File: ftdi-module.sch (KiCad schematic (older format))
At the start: 42 parts, among them J1 WE_629105150521, U1 FT2232HL-REEL, U2 NCP163ASN330T1G, Y1 KX-7_12,MHz

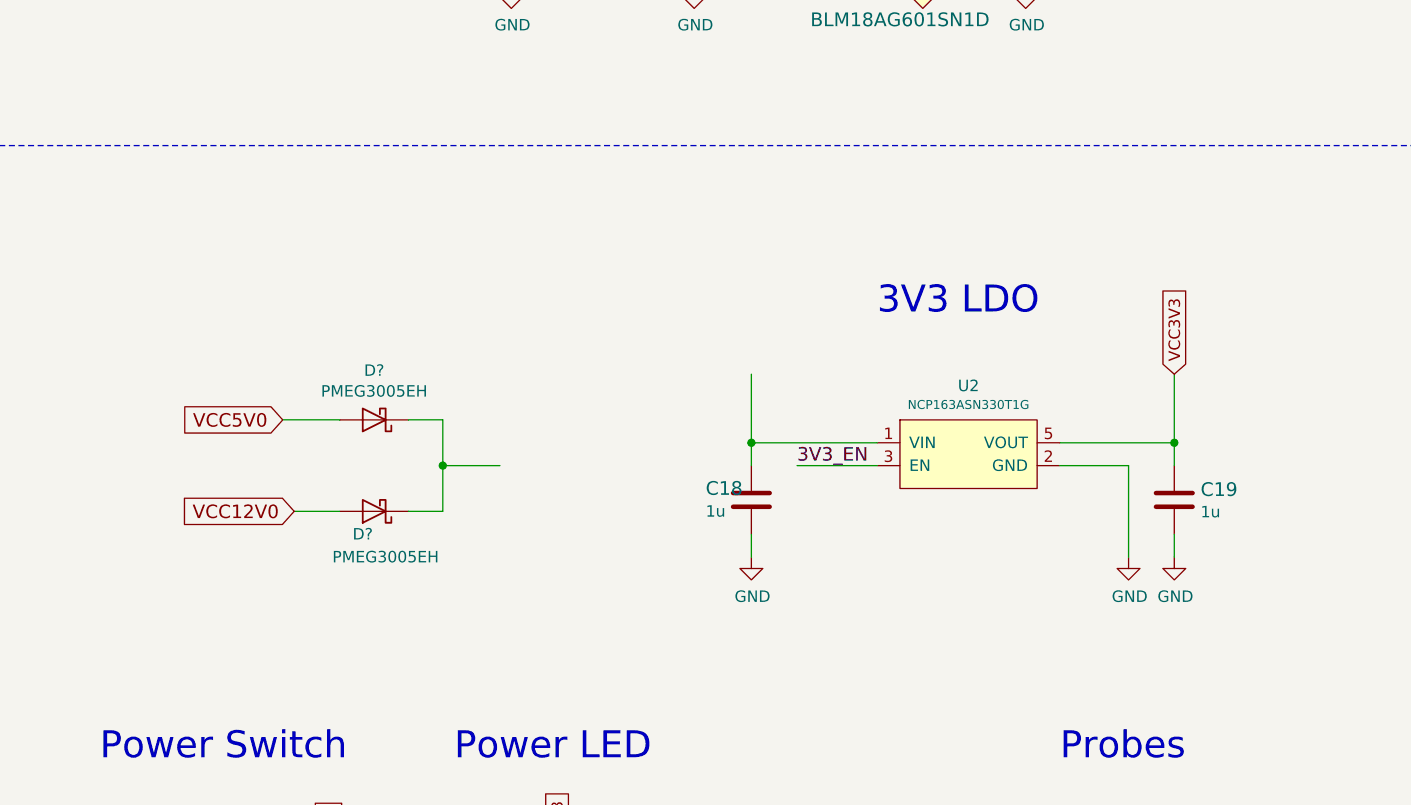
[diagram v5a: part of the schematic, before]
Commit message: Added connection between breakout boards
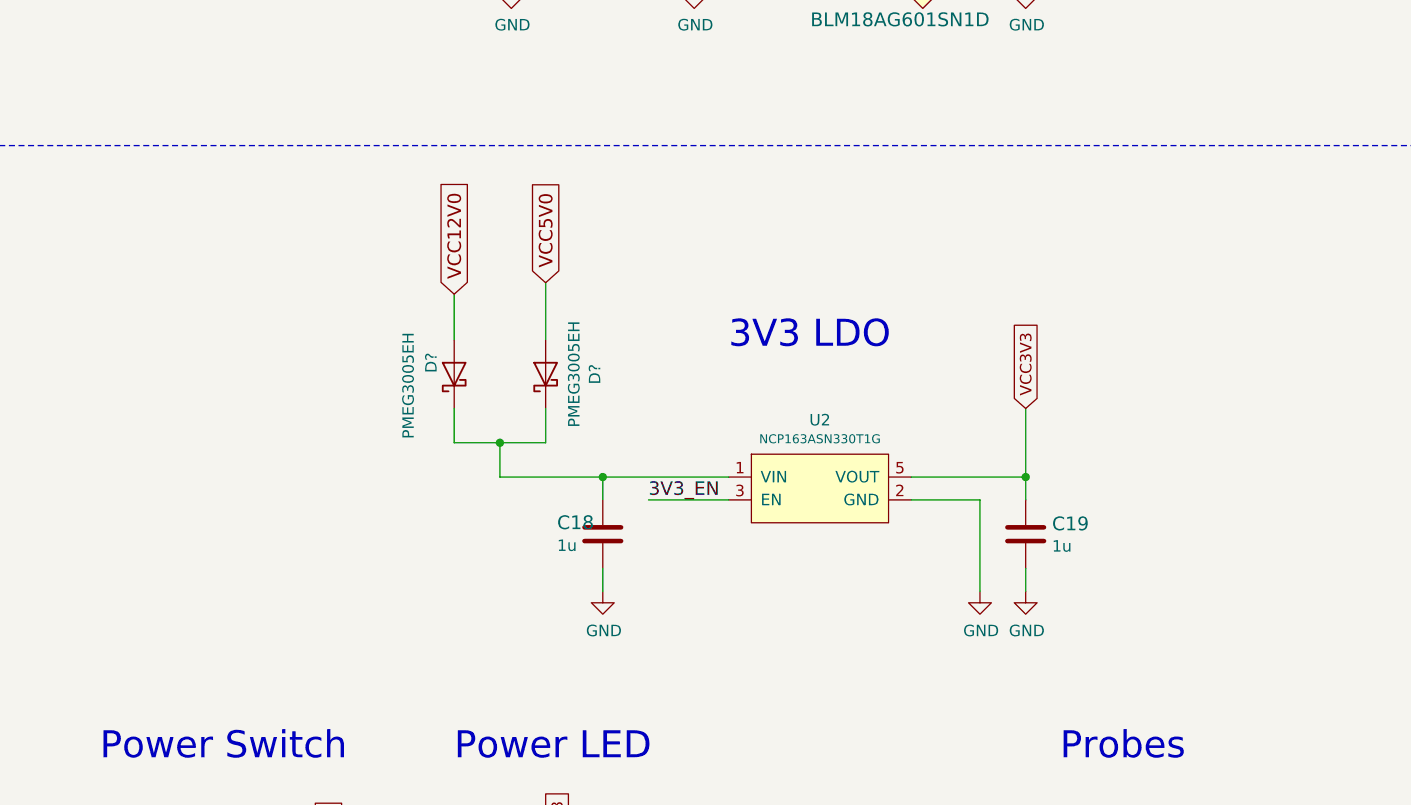
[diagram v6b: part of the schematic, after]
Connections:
- net at C18.1, U2.1 (VIN): now also D?.1 (K), D?.1 (K)
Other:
- moved on the sheet: C18, C19, D?, U2
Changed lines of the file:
@@
 $Descr A3 16535 11693
 encoding utf-8
-Sheet 2 3
+Sheet 2 4
 Title "NUC power breakout board - FTDI"
 Date "2022-03-04"
@@
 Wire Wire Line
 	14550 7650 14550 8000
-Text Notes 13000 4850 0    118  ~ 0
+Text Notes 12350 5000 0    118  ~ 0
 3V3 LDO
-Text GLabel 14300 5100 1    50   Input ~ 0
+Text GLabel 13650 5250 1    50   Input ~ 0
 VCC3V3
-Text GLabel 10450 5700 0    59   Input ~ 0
+Text GLabel 11150 4750 1    59   Input ~ 0
 VCC12V0
-Text GLabel 10400 5300 0    59   Input ~ 0
+Text GLabel 11550 4700 1    59   Input ~ 0
 VCC5V0
 $Comp
 L power:GND #PWR027
 U 1 1 624159A3
-P 12450 5900
-F 0 "#PWR027" H 12450 5650 50  0001 C CNN
-F 1 "GND" H 12455 5727 50  0000 C CNN
-F 2 "" H 12450 5900 50  0001 C CNN
-F 3 "" H 12450 5900 50  0001 C CNN
-	1    12450 5900
+P 11800 6050
+F 0 "#PWR027" H 11800 5800 50  0001 C CNN
+F 1 "GND" H 11805 5877 50  0000 C CNN
+F 2 "" H 11800 6050 50  0001 C CNN
+F 3 "" H 11800 6050 50  0001 C CNN
+	1    11800 6050
 	1    0    0    -1
 $EndComp
@@
 L antmicroCapacitors0402:C_1u_0402 C18
 U 1 1 6241C1A5
-P 12450 5650
-F 0 "C18" H 12250 5700 60  0000 L CNN
-F 1 "C_1u_0402" H 12450 5500 60  0001 C CNN
-F 2 "antmicro-footprints:0402-cap" H 12650 5850 60  0001 L CNN
-F 3 "" H 12450 5650 50  0001 C CNN
-F 4 "TDK" H 12650 6050 60  0001 L CNN "Manufacturer"
-F 5 "C1005X6S1A105K050BC" H 12650 5950 60  0001 L CNN "MPN"
-F 6 "1u" H 12250 5600 50  0000 L CNN "Val"
-	1    12450 5650
-	1    0    0    -1
-$EndComp
-Wire Wire Line
-	12450 5800 12450 5900
-Wire Wire Line
-	13000 5400 12450 5400
-Wire Wire Line
-	12450 5400 12450 5500
-Connection ~ 12450 5400
-Wire Wire Line
-	12450 5100 12450 5400
-Text Label 12650 5500 0    59   ~ 0
+P 11800 5800
+F 0 "C18" H 11600 5850 60  0000 L CNN
+F 1 "C_1u_0402" H 11800 5650 60  0001 C CNN
+F 2 "antmicro-footprints:0402-cap" H 12000 6000 60  0001 L CNN
+F 3 "" H 11800 5800 50  0001 C CNN
+F 4 "TDK" H 12000 6200 60  0001 L CNN "Manufacturer"
+F 5 "C1005X6S1A105K050BC" H 12000 6100 60  0001 L CNN "MPN"
+F 6 "1u" H 11600 5750 50  0000 L CNN "Val"
+	1    11800 5800
+	1    0    0    -1
+$EndComp
+Wire Wire Line
+	11800 5950 11800 6050
+Wire Wire Line
+	12350 5550 11800 5550
+Wire Wire Line
+	11800 5550 11800 5650
+Connection ~ 11800 5550
+Text Label 12000 5650 0    59   ~ 0
 3V3_EN
 Wire Wire Line
-	12650 5500 13000 5500
-Wire Wire Line
-	14300 5400 14300 5100
-Wire Wire Line
-	14300 5400 13800 5400
-Connection ~ 14300 5400
-Wire Wire Line
-	14300 5500 14300 5400
-Wire Wire Line
-	14300 5900 14300 5800
-Wire Wire Line
-	14100 5500 14100 5900
+	12000 5650 12350 5650
+Wire Wire Line
+	13650 5550 13650 5250
+Wire Wire Line
+	13650 5550 13150 5550
+Connection ~ 13650 5550
+Wire Wire Line
+	13650 5650 13650 5550
+Wire Wire Line
+	13650 6050 13650 5950
+Wire Wire Line
+	13450 5650 13450 6050
 $Comp
 L antmicroCapacitors0402:C_1u_0402 C19
 U 1 1 6241C482
-P 14300 5650
-F 0 "C19" H 14415 5695 60  0000 L CNN
-F 1 "C_1u_0402" H 14300 5500 60  0001 C CNN
-F 2 "antmicro-footprints:0402-cap" H 14500 5850 60  0001 L CNN
-F 3 "" H 14300 5650 50  0001 C CNN
-F 4 "TDK" H 14500 6050 60  0001 L CNN "Manufacturer"
-F 5 "C1005X6S1A105K050BC" H 14500 5950 60  0001 L CNN "MPN"
-F 6 "1u" H 14415 5597 50  0000 L CNN "Val"
-	1    14300 5650
-	1    0    0    -1
-$EndComp
-Wire Wire Line
-	14100 5500 13800 5500
+P 13650 5800
+F 0 "C19" H 13765 5845 60  0000 L CNN
+F 1 "C_1u_0402" H 13650 5650 60  0001 C CNN
+F 2 "antmicro-footprints:0402-cap" H 13850 6000 60  0001 L CNN
+F 3 "" H 13650 5800 50  0001 C CNN
+F 4 "TDK" H 13850 6200 60  0001 L CNN "Manufacturer"
+F 5 "C1005X6S1A105K050BC" H 13850 6100 60  0001 L CNN "MPN"
+F 6 "1u" H 13765 5747 50  0000 L CNN "Val"
+	1    13650 5800
+	1    0    0    -1
+$EndComp
+Wire Wire Line
+	13450 5650 13150 5650
 $Comp
 L power:GND #PWR030
 U 1 1 62416CD2
-P 14100 5900
-F 0 "#PWR030" H 14100 5650 50  0001 C CNN
-F 1 "GND" H 14105 5727 50  0000 C CNN
-F 2 "" H 14100 5900 50  0001 C CNN
-F 3 "" H 14100 5900 50  0001 C CNN
-	1    14100 5900
+P 13450 6050
+F 0 "#PWR030" H 13450 5800 50  0001 C CNN
+F 1 "GND" H 13455 5877 50  0000 C CNN
+F 2 "" H 13450 6050 50  0001 C CNN
+F 3 "" H 13450 6050 50  0001 C CNN
+	1    13450 6050
 	1    0    0    -1
 $EndComp
@@
 L power:GND #PWR031
 U 1 1 62416A2E
-P 14300 5900
-F 0 "#PWR031" H 14300 5650 50  0001 C CNN
-F 1 "GND" H 14305 5727 50  0000 C CNN
-F 2 "" H 14300 5900 50  0001 C CNN
-F 3 "" H 14300 5900 50  0001 C CNN
-	1    14300 5900
+P 13650 6050
+F 0 "#PWR031" H 13650 5800 50  0001 C CNN
+F 1 "GND" H 13655 5877 50  0000 C CNN
+F 2 "" H 13650 6050 50  0001 C CNN
+F 3 "" H 13650 6050 50  0001 C CNN
+	1    13650 6050
 	1    0    0    -1
 $EndComp
@@
 L antmicroPMICVoltageRegulatorsLinear:NCP163ASN330T1G U2
 U 1 1 62413EA1
-P 13400 5450
-F 0 "U2" H 13400 5749 50  0000 C CNN
-F 1 "NCP163ASN330T1G" H 13400 5666 39  0000 C CNN
-F 2 "antmicro-footprints:SOT-23-5" H 13400 5200 50  0001 C CNN
-F 3 "https://pl.mouser.com/datasheet/2/308/1/NCP163_D-2317108.pdf" H 13500 5800 50  0001 C CNN
-F 4 "NCP163ASN330T1G" H 13250 5750 50  0001 C CNN "MPN"
-F 5 "Onsemi" H 13350 5850 50  0001 C CNN "Manufacturer"
-	1    13400 5450
+P 12750 5600
+F 0 "U2" H 12750 5899 50  0000 C CNN
+F 1 "NCP163ASN330T1G" H 12750 5816 39  0000 C CNN
+F 2 "antmicro-footprints:SOT-23-5" H 12750 5350 50  0001 C CNN
+F 3 "https://pl.mouser.com/datasheet/2/308/1/NCP163_D-2317108.pdf" H 12850 5950 50  0001 C CNN
+F 4 "NCP163ASN330T1G" H 12600 5900 50  0001 C CNN "MPN"
+F 5 "Onsemi" H 12700 6000 50  0001 C CNN "Manufacturer"
+	1    12750 5600
 	1    0    0    -1
 $EndComp
@@
 L Diode:PMEG3005EH D?
 U 1 1 6245583F
-P 10800 5300
-F 0 "D?" H 10800 5084 50  0000 C CNN
-F 1 "PMEG3005EH" H 10800 5175 50  0000 C CNN
-F 2 "Diode_SMD:D_SOD-123F" H 10800 5125 50  0001 C CNN
-F 3 "https://assets.nexperia.com/documents/data-sheet/PMEGXX05EH_EJ_SER.pdf" H 10800 5300 50  0001 C CNN
-	1    10800 5300
-	-1   0    0    1
+P 11550 5100
+F 0 "D?" H 11550 4884 50  0000 C CNN
+F 1 "PMEG3005EH" H 11550 4975 50  0000 C CNN
+F 2 "Diode_SMD:D_SOD-123F" H 11550 4925 50  0001 C CNN
+F 3 "https://assets.nexperia.com/documents/data-sheet/PMEGXX05EH_EJ_SER.pdf" H 11550 5100 50  0001 C CNN
+	1    11550 5100
+	0    -1   -1   0
 $EndComp
 $Comp
 L Diode:PMEG3005EH D?
 U 1 1 624568EB
-P 10800 5700
-F 0 "D?" H 10850 5800 50  0000 C CNN
-F 1 "PMEG3005EH" H 10750 5900 50  0000 C CNN
-F 2 "Diode_SMD:D_SOD-123F" H 10800 5525 50  0001 C CNN
-F 3 "https://assets.nexperia.com/documents/data-sheet/PMEGXX05EH_EJ_SER.pdf" H 10800 5700 50  0001 C CNN
-	1    10800 5700
-	-1   0    0    1
-$EndComp
-Wire Wire Line
-	10450 5700 10650 5700
-Wire Wire Line
-	10950 5700 11100 5700
-Wire Wire Line
-	11100 5700 11100 5500
-Wire Wire Line
-	11100 5500 11350 5500
-Wire Wire Line
-	10400 5300 10650 5300
-Wire Wire Line
-	10950 5300 11100 5300
-Wire Wire Line
-	11100 5300 11100 5500
-Connection ~ 11100 5500
+P 11150 5100
+F 0 "D?" H 11200 5200 50  0000 C CNN
+F 1 "PMEG3005EH" H 11100 5300 50  0000 C CNN
+F 2 "Diode_SMD:D_SOD-123F" H 11150 4925 50  0001 C CNN
+F 3 "https://assets.nexperia.com/documents/data-sheet/PMEGXX05EH_EJ_SER.pdf" H 11150 5100 50  0001 C CNN
+	1    11150 5100
+	0    -1   -1   0
+$EndComp
+Wire Wire Line
+	11150 4750 11150 4950
+Wire Wire Line
+	11150 5250 11150 5400
+Wire Wire Line
+	11550 4700 11550 4950
+Wire Wire Line
+	11550 5250 11550 5400
+Wire Wire Line
+	11150 5400 11350 5400
+Wire Wire Line
+	11350 5400 11350 5550
+Connection ~ 11350 5400
+Wire Wire Line
+	11350 5400 11550 5400
+Wire Wire Line
+	11350 5550 11800 5550
 $EndSCHEMATC

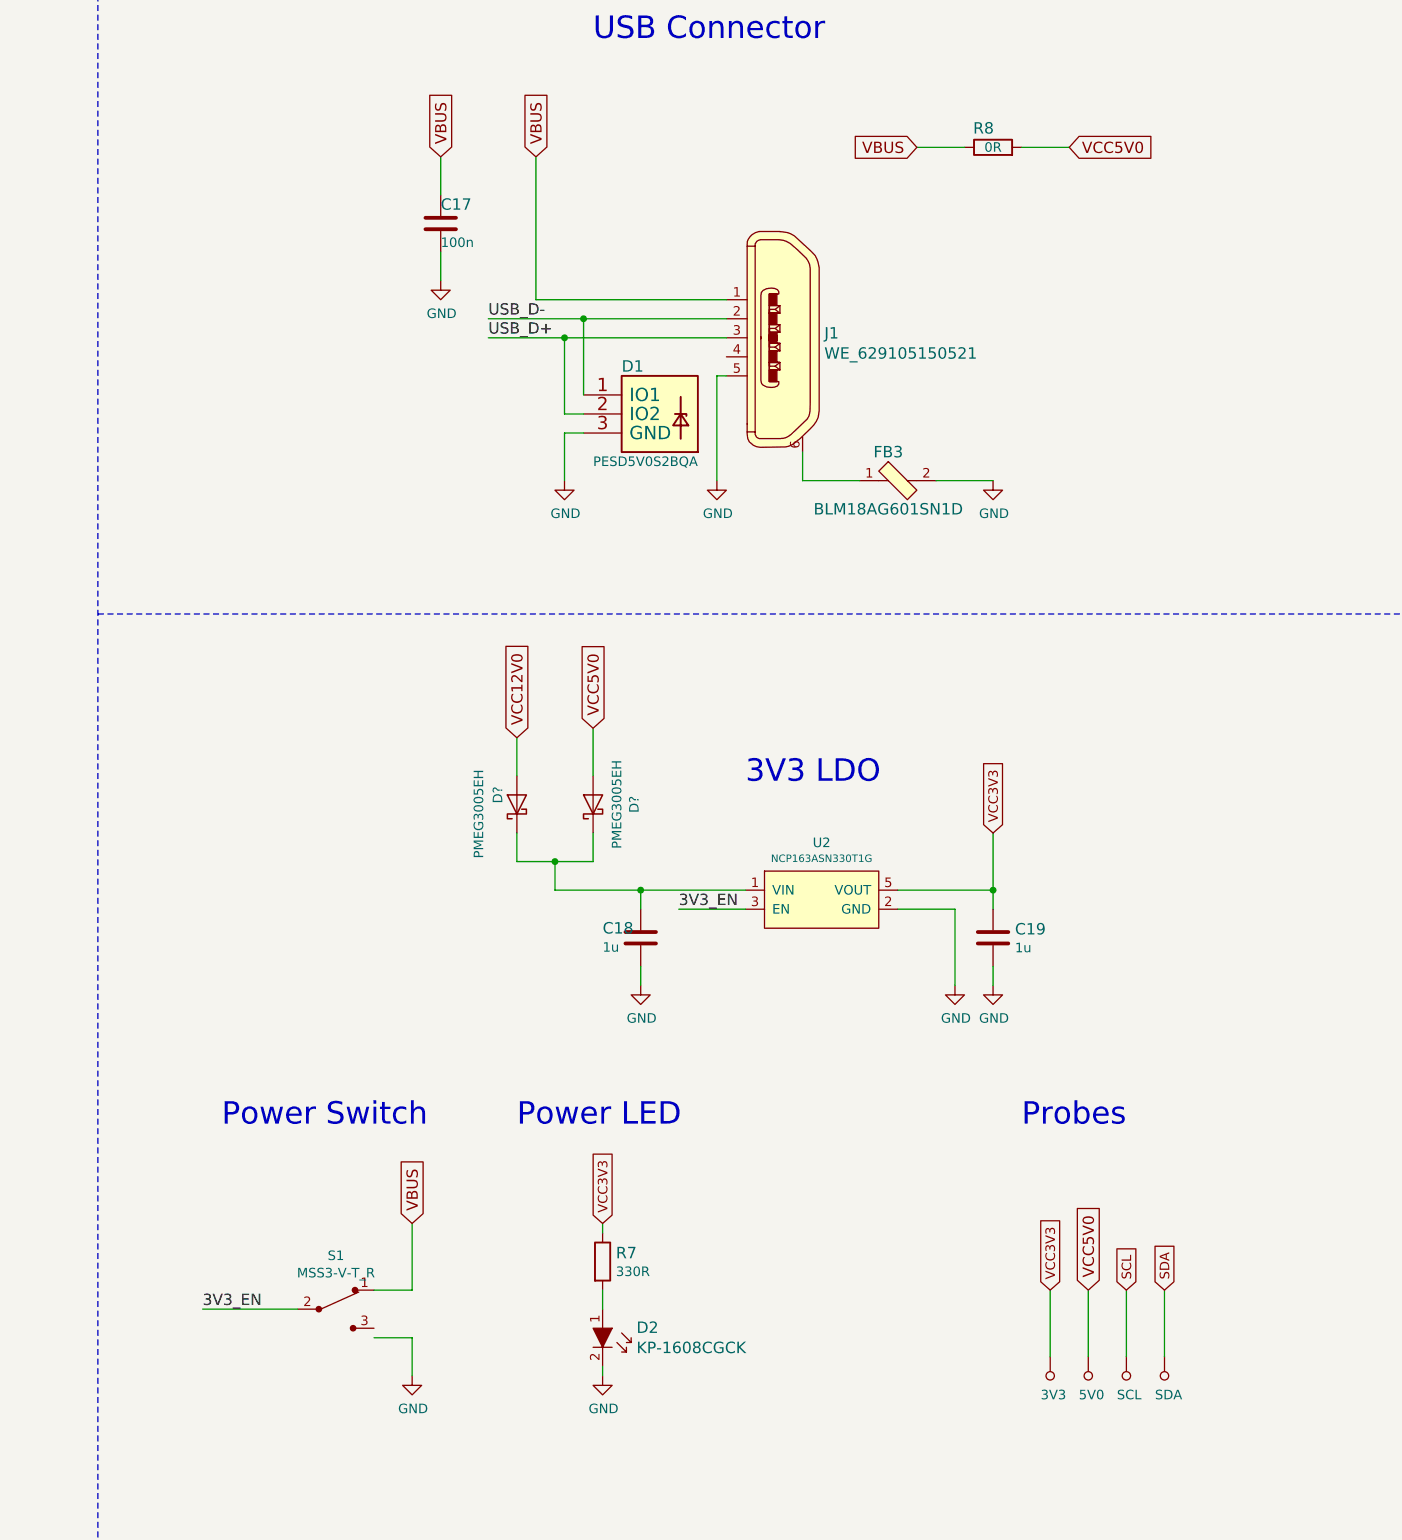
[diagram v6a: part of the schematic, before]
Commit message: Schematic improvements according to review's comments
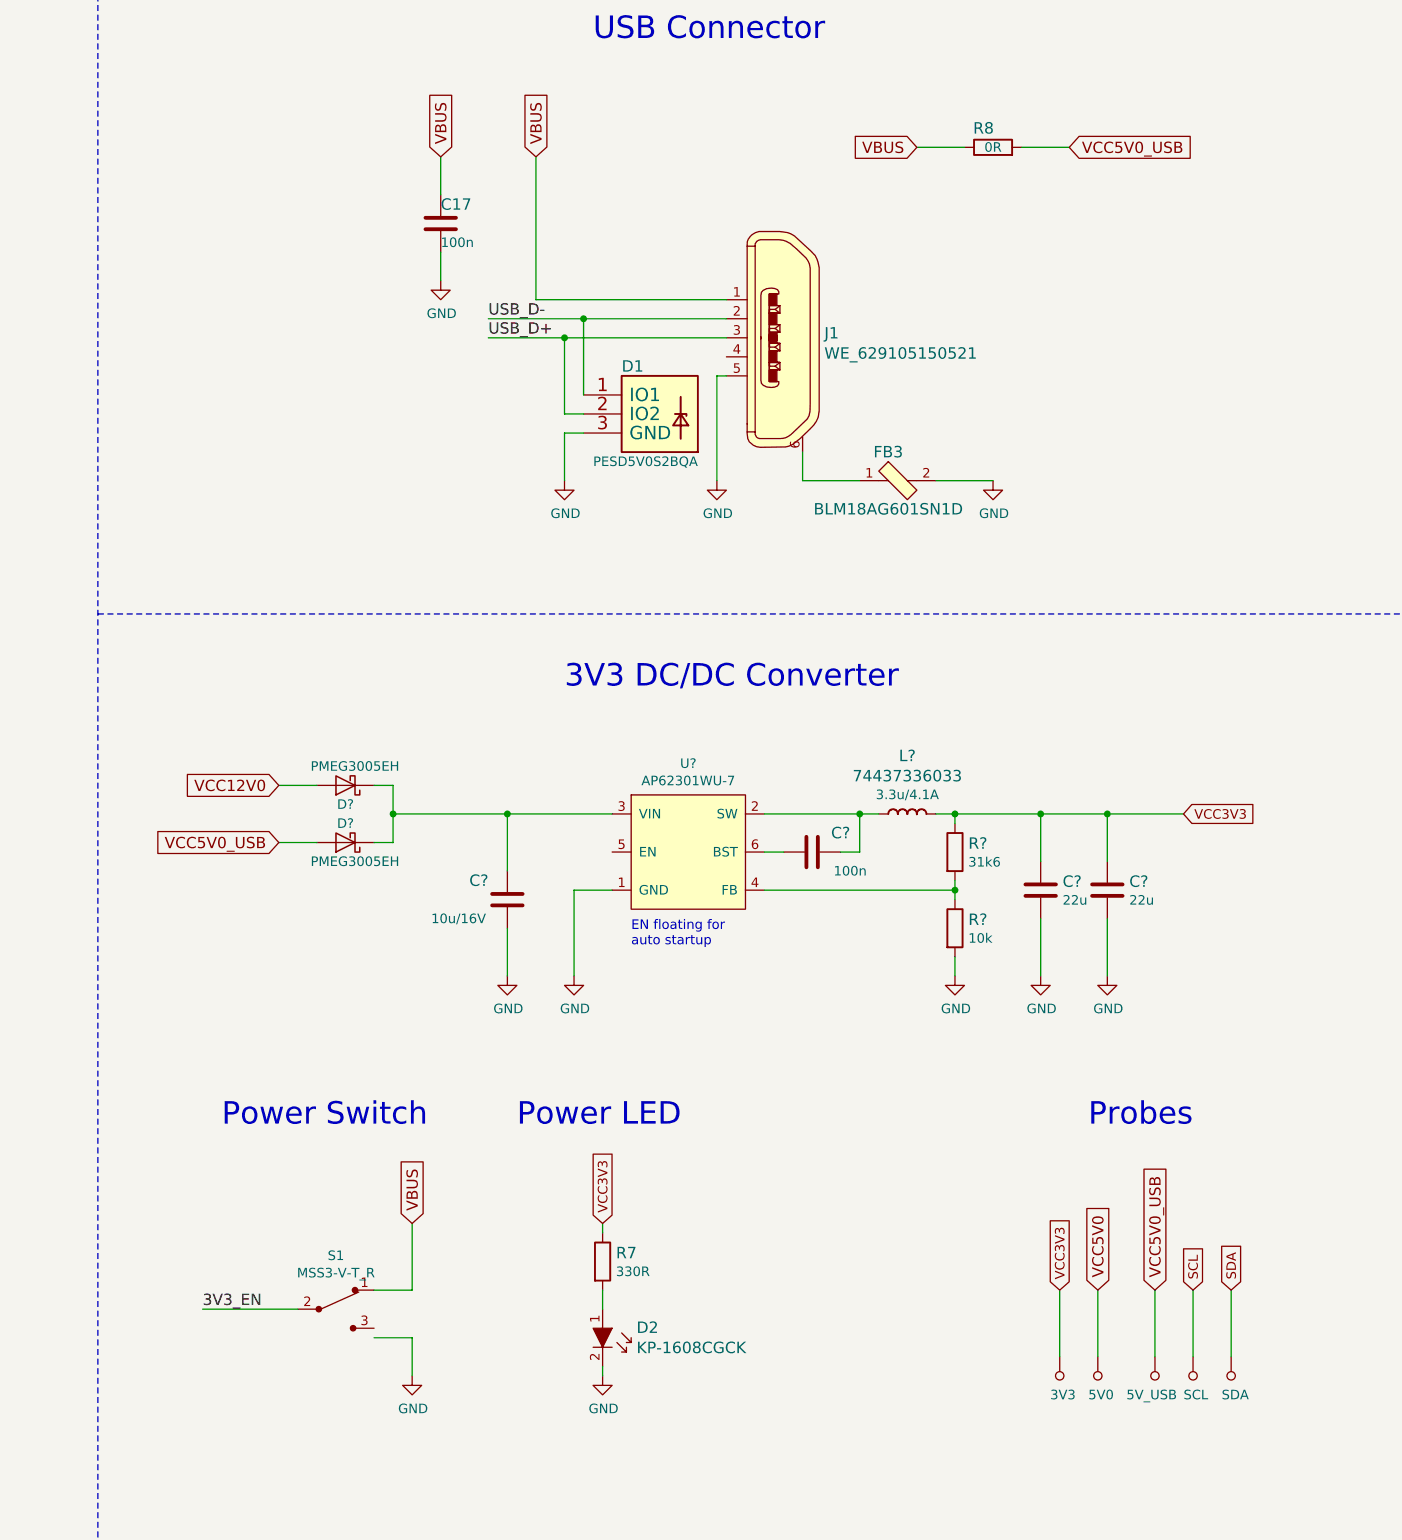
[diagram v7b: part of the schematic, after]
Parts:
- removed C18, C19: C_1u_0402, antmicro-footprints:0402-cap, symbol antmicroCapacitors0402:C_1u_0402
- removed U2: NCP163ASN330T1G, antmicro-footprints:SOT-23-5, symbol antmicroPMICVoltageRegulatorsLinear:NCP163ASN330T1G
- added 5V_USB: TP_SMD1MM, antmicro-footprints:Testpoint_smd_1mm, symbol antmicroTestPoints:TP_SMD1MM
- added C?: C_100n_0402, antmicro-footprints:0402-cap, symbol antmicroCapacitors0402:C_100n_0402
- added C? (x2): C_22u_0603, antmicro-footprints:0603-cap, symbol antmicroCapacitors0603:C_22u_0603
- added C?: C_10u_16V_0603, antmicro-footprints:0603-cap, symbol antmicroCapacitors0603:C_10u_16V_0603
- added L?: 74437336033, antmicro-footprints:WE_74437336033, symbol antmicroFixedInductors:74437336033
- added R?: R_31k6_0402, antmicro-footprints:0402-res, symbol antmicroResistors0402:R_31k6_0402
- added R?: R_10k_0402, antmicro-footprints:0402-res, symbol antmicroResistors0402:R_10k_0402
- added U?: AP62301WU-7, antmicro-footprints:TSOT23-6, symbol antmicroDCDCConverters:AP62301WU-7
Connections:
- net GND: now also C?.2, C?.2, C?.2, R?.2, U?.1 (GND)
- net VCC12V0: now also D?.2 (A); no longer D?.2 (A)
- net VCC3V3: now also C?.1, C?.1, L?.2 (P), R?.1
- net VCC5V0: no longer D?.2 (A), R8.2
- net at D?.1 (K), D?.1 (K): now also C?.1, U?.3 (VIN)
- new net: C?.1, L?.1 (P), U?.2 (SW)
- new net: R?.1, R?.2, U?.4 (FB)
- new net: C?.2, U?.6 (BST)
- new net VCC5V0_USB: 5V_USB.1, D?.2 (A), R8.2
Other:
- note added: "3V3 DC/DC Converter"
- note added: "EN floating for \nauto startup\n"
- note removed: "3V3 LDO"
- moved on the sheet: 3V3, 5V0, D?, SCL, SDA
